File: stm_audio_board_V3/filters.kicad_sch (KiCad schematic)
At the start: 25 parts

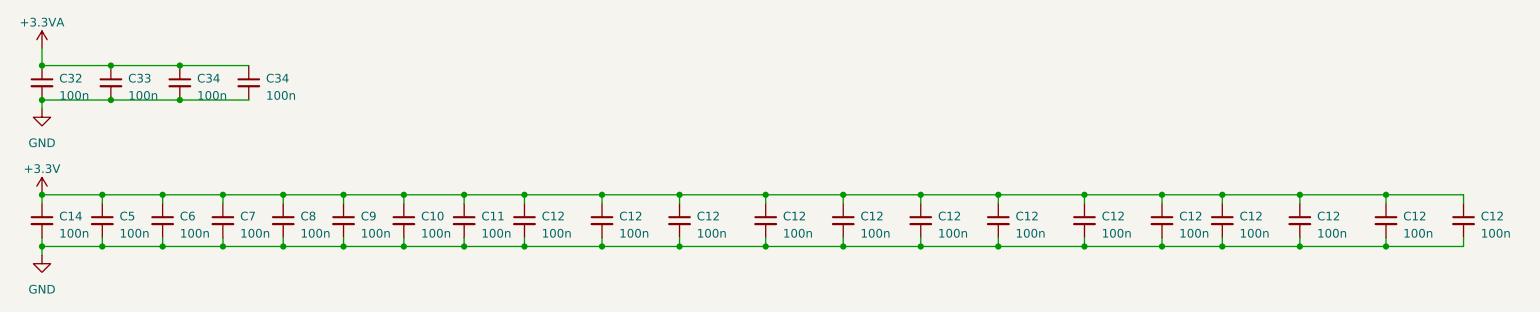
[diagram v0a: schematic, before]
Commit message: minor changes to components
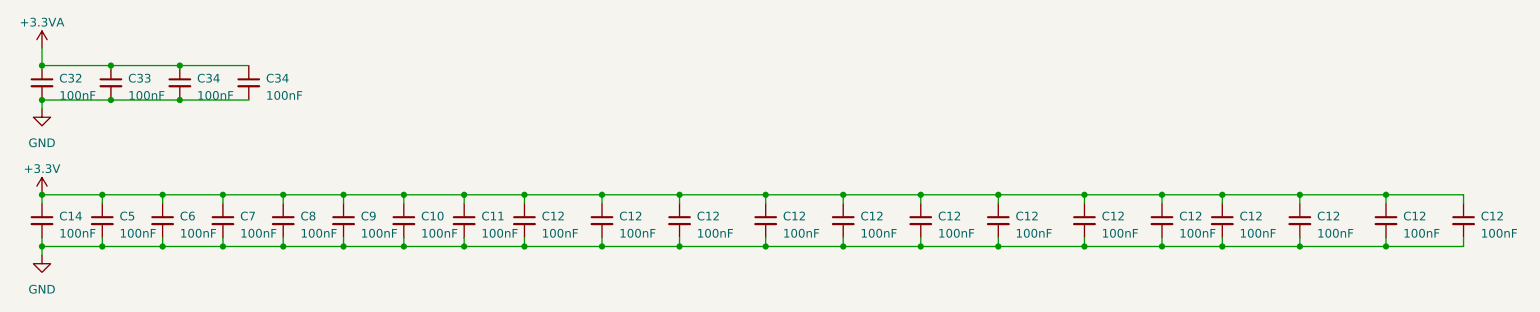
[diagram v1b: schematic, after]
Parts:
- C10, C11, C12, C14, C32, C33, C34, C5, C6, C7, C8, C9: value 100n -> 100nF; JLCPCB (none) -> C14663; LCSC Part (none) -> C14663
